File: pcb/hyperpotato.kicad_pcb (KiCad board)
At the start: 2 copper layers, 117.8 x 93.2 mm, 71 parts, among them J1 Conn_01x02_Socket, J2 Conn_01x02_Socket, J3 Conn_01x04, J4 Conn_01x04, J5 Conn_01x04, J6 Conn_01x12_Socket, J7 Conn_01x12_Socket, K1 SW_Push, K10 SW_Push, K11 SW_Push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

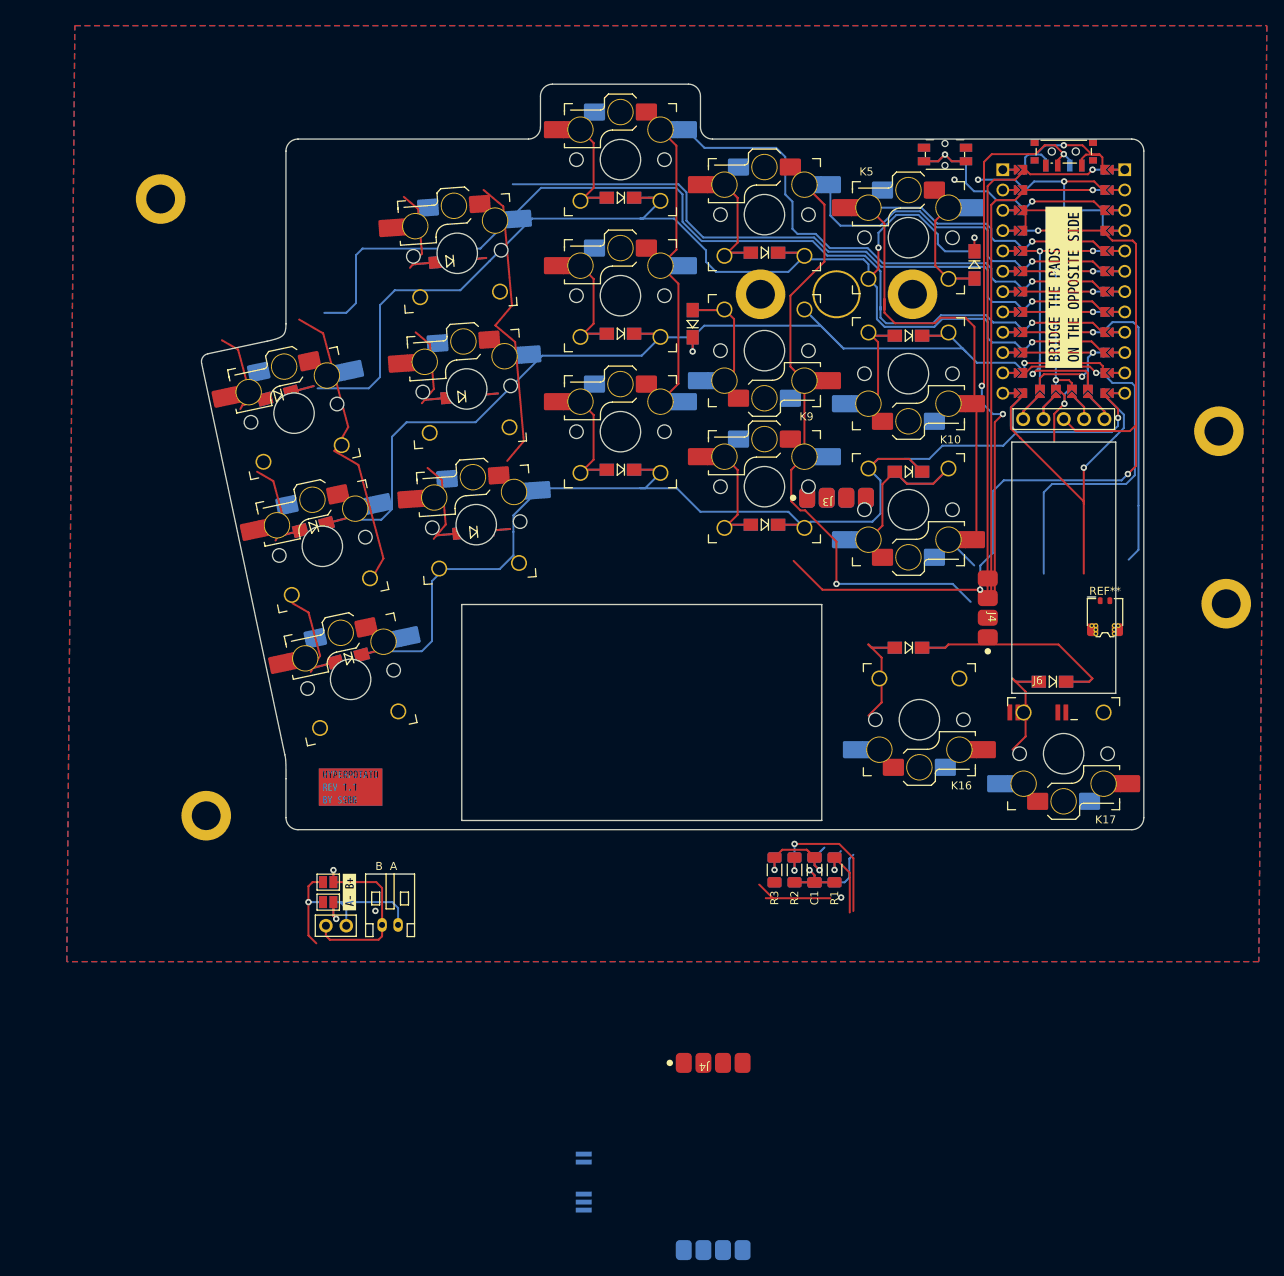
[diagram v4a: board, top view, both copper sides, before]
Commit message: Distribute components
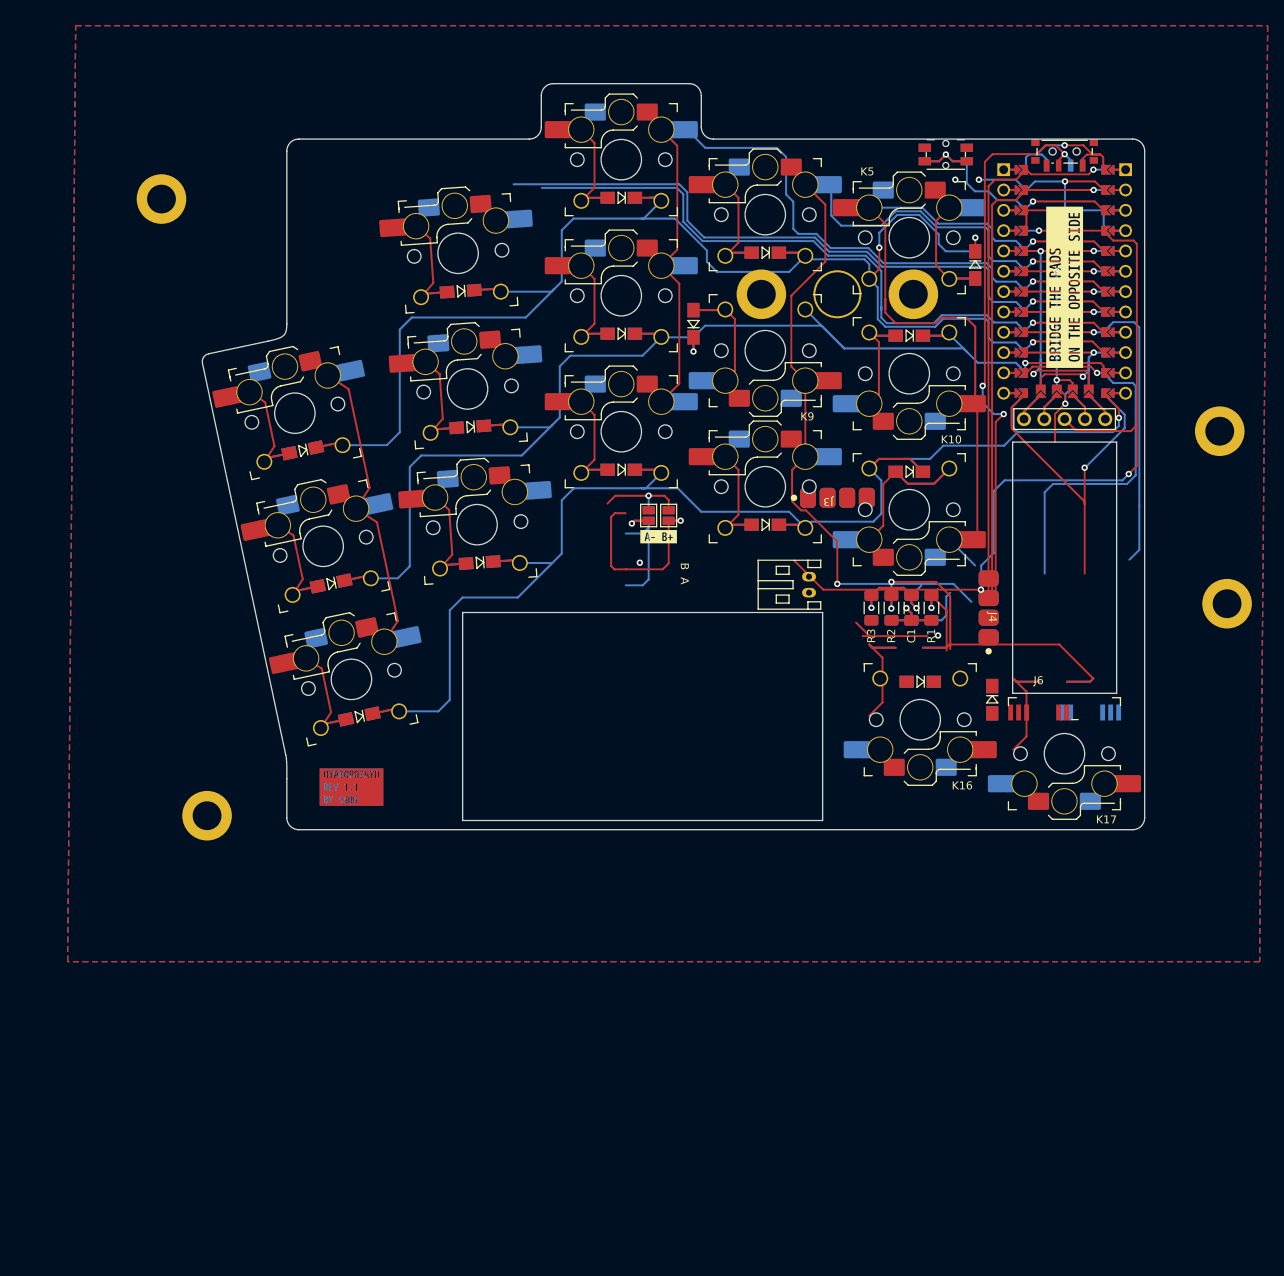
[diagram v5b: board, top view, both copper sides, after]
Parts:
- removed J1: Conn_01x02_Socket, hyperpotato:PinHeader_1x02_P2.54mm_Vertical
- removed the J4 at (120.6, 150.9)
- removed the REF** at (169.5, 94.9)
- K17: footprint hyperpotato:V1_V2_HS_reversible_plated -> hyperpotato:V1_V2_HS_reversible_plated_no_fix_pin
- moved J5 87.3 mm to (154.9, 94.0), turned to 0 degrees
- moved J7 86.4 mm to (167.7, 107.0), turned to 180 degrees
- moved J2 67.3 mm to (132.5, 90.1), turned to -90 degrees
- moved JP5 62.8 mm to (112.5, 82.4), turned to 90 degrees
- moved JP6 62.8 mm to (112.5, 82.4), turned to 90 degrees
- moved JP7 62.5 mm to (115.0, 82.4), turned to 90 degrees
- moved JP8 62.5 mm to (115.0, 82.4), turned to 90 degrees
- moved kibuzzard-65B4826D 58.9 mm to (113.7, 85.1), turned to 0 degrees
- moved kibuzzard-65B482C9 58.9 mm to (113.7, 85.1), turned to 180 degrees
- moved C1 34.9 mm to (145.3, 94.0)
- moved R2 34.9 mm to (142.8, 94.0)
- moved R3 34.9 mm to (140.3, 94.0)
- moved R1 34.9 mm to (147.8, 94.0)
- moved D17 7.86 mm to (155.4, 105.4), turned to -90 degrees
- moved D1 7.51 mm to (69.3, 74.3), turned to -168 degrees
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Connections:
- J4 pad 1: (no net) -> Net-(J3-Pin_1)
- J4 pad 2: (no net) -> Net-(J3-Pin_2)
- J4 pad 3: (no net) -> Net-(J3-Pin_3)
- J4 pad 4: (no net) -> Net-(J3-Pin_4)
- U1 pad 11: ENC_A -> unconnected-(U1-8/B4-Pad11)
- U1 pad 12: ENC_B -> unconnected-(U1-9/B5-Pad12)
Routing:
- net ENC_A: track 48.6 -> 0.00 mm, vias 1 -> 0
- net unconnected-(U1-8/B4-Pad11): track 0.00 -> 48.6 mm, vias 0 -> 1
- net unconnected-(U1-9/B5-Pad12): track 0.00 -> 44.1 mm, vias 0 -> 1
- net ENC_B: track 44.1 -> 0.00 mm, vias 1 -> 0
- net COL1: track 123.5 -> 85.8 mm
- net COL0: track 160.2 -> 122.7 mm
- net ROW3: track 78.1 -> 51.4 mm
- net Net-(J3-Pin_1): track 0.00 -> 26.7 mm
- net ROW0: track 178.1 -> 193.0 mm
- net ROW1: track 149.8 -> 163.9 mm
- net TP_PCB_RESET: track 15.7 -> 29.4 mm
- net Net-(D17-A): track 17.2 -> 3.47 mm
- net ROW2: track 168.2 -> 179.9 mm
- net Net-(D16-A): track 17.2 -> 27.7 mm
- net Net-(J3-Pin_2): track 10.5 -> 0.00 mm
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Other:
- board size 117.8 x 93.2 mm -> 117.8 x 93.3 mm
